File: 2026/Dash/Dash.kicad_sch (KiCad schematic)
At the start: 88 parts, among them IC1 ESP32-S3-WROOM-1-N8R8, IC2 CP2102N-A02-GQFN28, IC3 TLP175A_TPL,E, IC4 TPS2116DRLR, IC5 MIC37100-3.3WS, IC6 TLC5955RTQT, IC7 TLC5955RTQT, J2 USB_C_Receptacle_USB2.0_16P, J5 Conn_01x40_Pin, Q1 MMBT2222LT1G, Q2 MMBT2222LT1G, U1 USBLC6-2SC6, U2 SN65HVD230

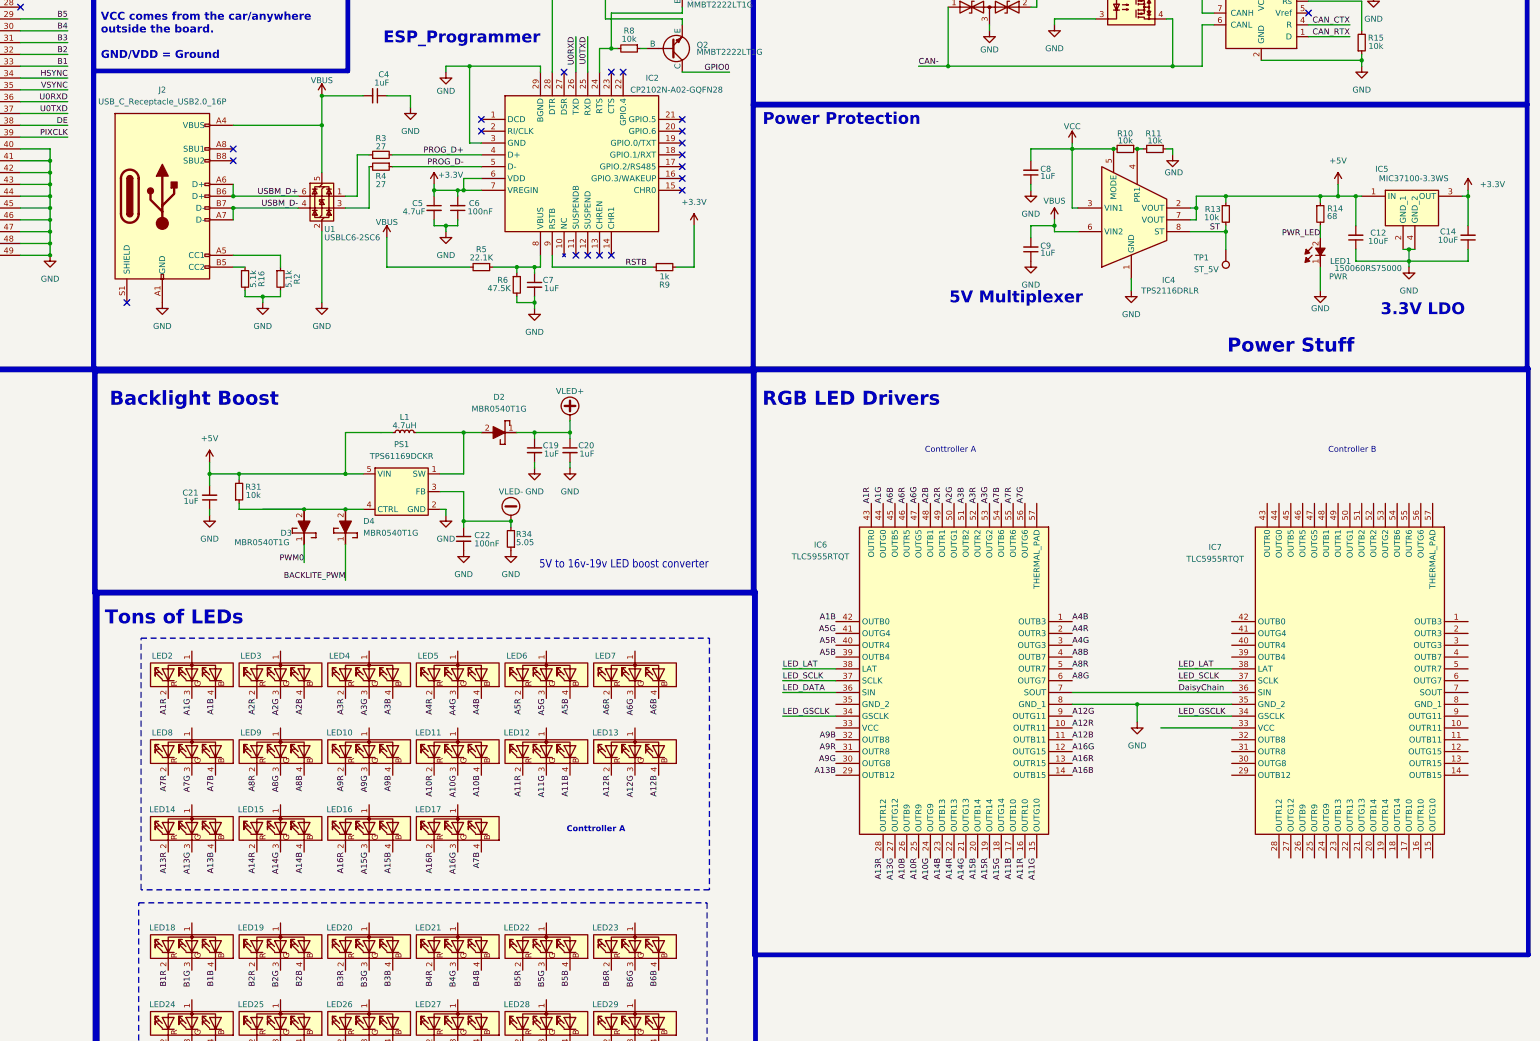
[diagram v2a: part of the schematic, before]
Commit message: Changed dash to IP67 USB C
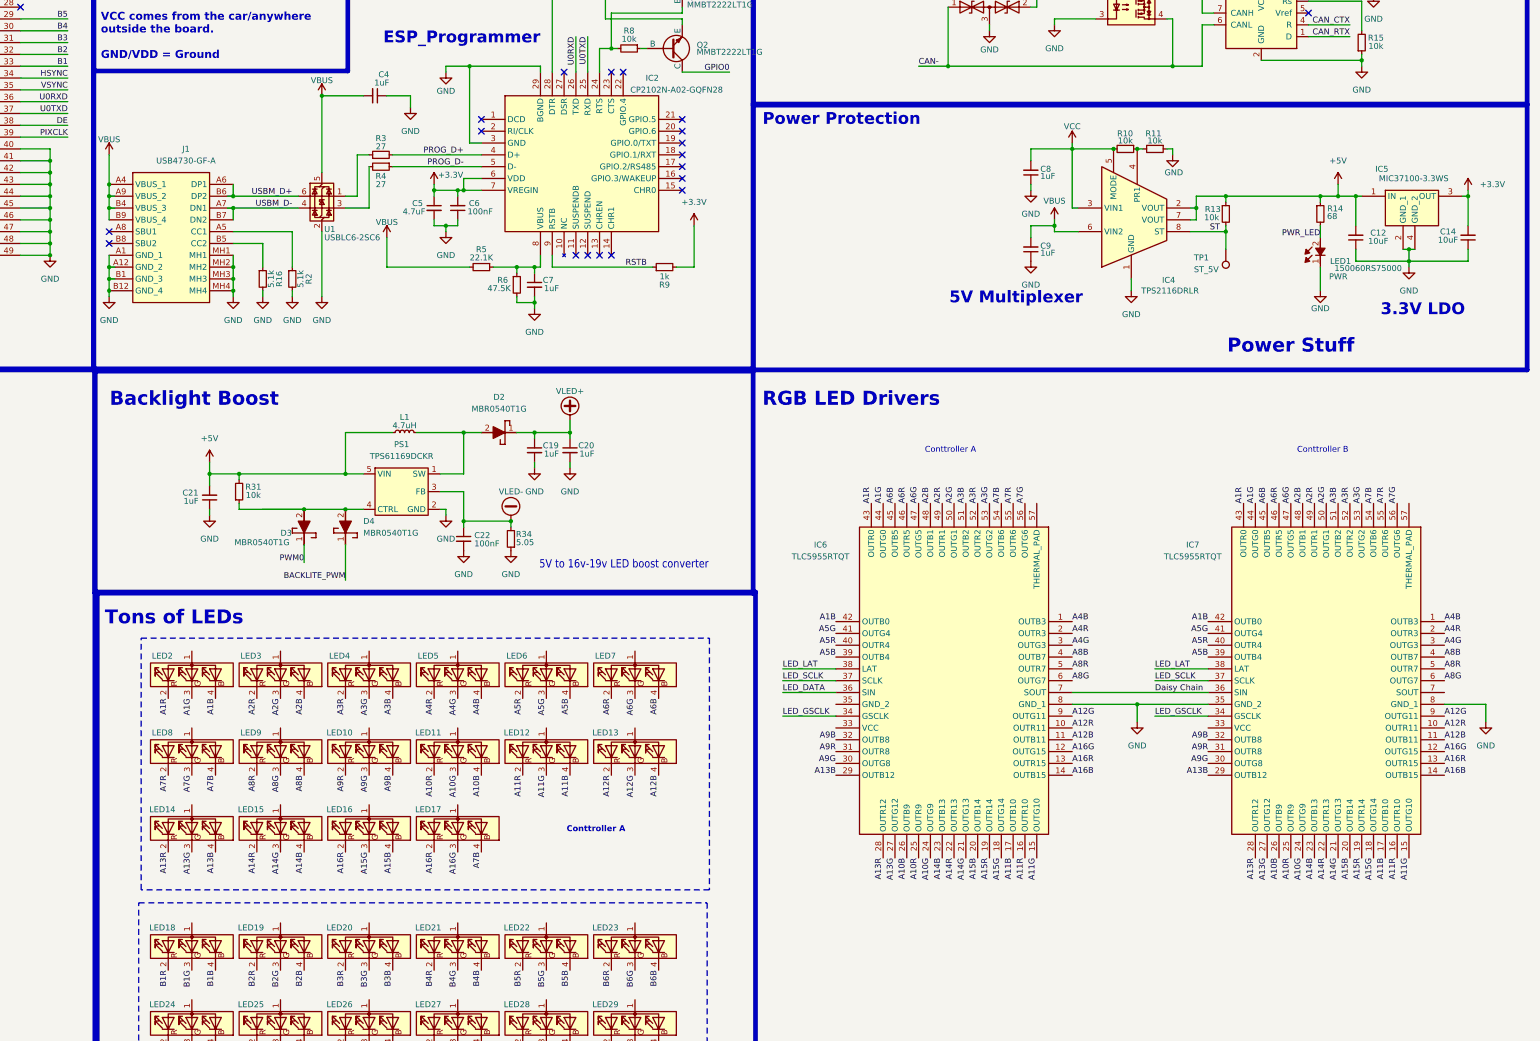
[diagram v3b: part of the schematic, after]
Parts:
- removed J2: USB_C_Receptacle_USB2.0_16P, SDM_MiscFootprint:USB_C_Receptacle_16P, symbol Connector:USB_C_Receptacle_USB2.0_16P
- added J1: USB4730-GF-A, USB4730GFA, symbol SDM_CONNECTOR:USB4730-GF-A
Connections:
- net A10B: now also IC7.26 (OUTB9)
- net A10G: now also IC7.24 (OUTG9)
- net A10R: now also IC7.25 (OUTR9)
- net A11B: now also IC7.17 (OUTB10)
- net A11G: now also IC7.15 (OUTG10)
- net A11R: now also IC7.16 (OUTR10)
- net A12B: now also IC7.11 (OUTB11)
- net A12G: now also IC7.9 (OUTG11)
- net A12R: now also IC7.10 (OUTR11)
- net A13B: now also IC7.29 (OUTB12)
- net A13G: now also IC7.27 (OUTG12)
- net A13R: now also IC7.28 (OUTR12)
- net A14B: now also IC7.23 (OUTB13)
- net A14G: now also IC7.21 (OUTG13)
- net A14R: now also IC7.22 (OUTR13)
- net A15B: now also IC7.20 (OUTB14)
- net A15G: now also IC7.18 (OUTG14)
- net A15R: now also IC7.19 (OUTR14)
- net A16B: now also IC7.14 (OUTB15)
- net A16G: now also IC7.12 (OUTG15)
- net A16R: now also IC7.13 (OUTR15)
- net A1B: now also IC7.42 (OUTB0)
- net A1G: now also IC7.44 (OUTG0)
- net A1R: now also IC7.43 (OUTR0)
- net A2B: now also IC7.48 (OUTB1)
- net A2G: now also IC7.50 (OUTG1)
- net A2R: now also IC7.49 (OUTR1)
- net A3B: now also IC7.51 (OUTB2)
- net A3G: now also IC7.53 (OUTG2)
- net A3R: now also IC7.52 (OUTR2)
- net A4B: now also IC7.1 (OUTB3)
- net A4G: now also IC7.3 (OUTG3)
- net A4R: now also IC7.2 (OUTR3)
- net A5B: now also IC7.39 (OUTB4)
- net A5G: now also IC7.41 (OUTG4)
- net A5R: now also IC7.40 (OUTR4)
- net A6B: now also IC7.45 (OUTB5)
- net A6G: now also IC7.47 (OUTG5)
- net A6R: now also IC7.46 (OUTR5)
- net A7B: now also IC7.54 (OUTB6)
- net A7G: now also IC7.56 (OUTG6)
- net A7R: now also IC7.55 (OUTR6)
- net A8B: now also IC7.4 (OUTB7)
- net A8G: now also IC7.6 (OUTG7)
- net A8R: now also IC7.5 (OUTR7)
- net A9B: now also IC7.32 (OUTB8)
- net A9G: now also IC7.30 (OUTG8)
- net A9R: now also IC7.31 (OUTR8)
- net GND: now also IC7.8 (GND_1), J1.A1 (GND_1), J1.A12 (GND_2), J1.B1 (GND_3), J1.B12 (GND_4), J1.MH1, J1.MH2, J1.MH3, J1.MH4
- net USBM_D+: now also J1.A6 (DP1), J1.B6 (DP2)
- net USBM_D-: now also J1.A7 (DN1), J1.B7 (DN2)
- net VBUS: now also J1.A4 (VBUS_1), J1.A9 (VBUS_2), J1.B4 (VBUS_3), J1.B9 (VBUS_4)
- net at R2.1: now also J1.A5 (CC1)
- net at R16.1: now also J1.B5 (CC2)
- net DaisyChain renamed Daisy Chain
- no-connect marks 24 -> 23
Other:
- note added: "Conttroller B"
- moved on the sheet: R2

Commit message: Dash progress
added to libs and swaped dash to BT818. Work in progress
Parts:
- removed J5: Conn_01x40_Pin, Connector_FFC-FPC:Omron_XF2M-4015-1A_1x40-1MP_P0.5mm_Horizontal, symbol Connector:Conn_01x40_Pin
- added C10: O.1uF, Capacitor_SMD:C_0603_1608Metric, symbol Device:C_Small
- added IC8: BT818Q-T, SDM_MiscFootprint:QFN50P900X900X90-65N-D, symbol SDM_CONNECTOR:BT818Q-T
- added IC9: S25FL256LAGNFB010, SDM_MiscFootprint:SON127P600X500X80-9N-D, symbol SDM_CONNECTOR:S25FL256LAGNFB010
- added J2: Conn_01x40_Pin, Connector_FFC-FPC:Omron_XF2M-4015-1A_1x40-1MP_P0.5mm_Horizontal, symbol Connector:Conn_01x40_Pin
- added J4: Molex_1040310811, Connector_Card:microSD_HC_Molex_104031-0811, symbol Connector:Micro_SD_Card_Det2
- added R17, R18, R19, R20, R21, R22, R23, R24, R25, R26, R27, R28, R29, R30, R32, R33, R35, R36, R37, R38, R39, R40, R41, R42, R43, R44, R45, R46, R47, R48, R49, R50, R52, R53: 33, Resistor_SMD:R_0603_1608Metric, symbol Device:R_Small
- added R51: 47K, Resistor_SMD:R_0603_1608Metric, symbol Device:R_Small
- added U10: EMIF06-MSD02N16, SDM_MiscFootprint:UQFN-17-3.5x1.2mm_copy, symbol lib:ST_EMIF06-MSD02N16
- J1: footprint USB4730GFA -> SDM_MiscFootprint:USB4730GFA
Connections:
- net SD_MISO is gone; now on net SD_CS: IC1.8 (IO15)
- net +3.3V: now also C10.2, IC8.17 (VCCIO3), IC9.8 (VCC), J2.4 (Pin_4), J4.4 (VDD), R51.2, U10.15 (VCC), U10.16 (RDATA_VCC)
- net B1: now also J2.22 (Pin_22), R20.2; no longer IC1.33 (IO40)
- net B2: now also J2.23 (Pin_23), R24.2; no longer IC1.32 (IO39)
- net B3: now also J2.24 (Pin_24), R25.2; no longer IC1.31 (IO38)
- net B4: now also J2.25 (Pin_25), R26.2; no longer IC1.30 (IO37)
- net B5: now also J2.26 (Pin_26), R27.2; no longer IC1.29 (IO36)
- net BACKLITE_PWM: now also IC8.34 (BACKLIGHT)
- net DE: now also IC8.35 (DE), J2.34 (Pin_34); no longer IC1.38 (IO2)
- net G0: now also J2.13 (Pin_13), R39.2; no longer IC1.25 (IO48)
- net G1: now also J2.14 (Pin_14), R38.2; no longer IC1.24 (IO47)
- net G2: now also J2.15 (Pin_15), R37.2; no longer IC1.23 (IO21)
- net G3: now also J2.16 (Pin_16), R36.2; no longer IC1.22 (IO14)
- net G4: now also J2.17 (Pin_17), R35.2; no longer IC1.21 (IO13)
- net G5: now also J2.18 (Pin_18), R33.2; no longer IC1.20 (IO12)
- net GND: now also C10.1, IC9.4 (VSS), IC9.9 (EP), J2.29 (Pin_29), J2.3 (Pin_3), J2.36 (Pin_36), J4.11 (SHIELD), J4.6 (VSS), J4.9 (DET_B), U10.17 (GND)
- net HSYNC: now also IC8.37 (HSYNC), J2.32 (Pin_32); no longer IC1.34 (IO41)
- net PIXCLK: now also IC8.39 (PCLK), J2.30 (Pin_30); no longer IC1.39 (IO1)
- net R1: now also J2.6 (Pin_6), R46.2; no longer IC1.19 (IO11)
- net R2: now also J2.7 (Pin_7), R45.2; no longer IC1.18 (IO10)
- net R3: now also J2.8 (Pin_8), R44.2; no longer IC1.17 (IO9)
- net R4: now also J2.9 (Pin_9), R43.2; no longer IC1.16 (IO46)
- net R5: now also J2.10 (Pin_10), R42.2; no longer IC1.15 (IO3)
- net SD_CS: no longer IC1.9 (IO16)
- net VLED+: now also J2.2 (Pin_2)
- net VLED-: now also J2.1 (Pin_1)
- net VSYNC: now also IC8.36 (VSYNC), J2.33 (Pin_33); no longer IC1.35 (IO42)
- net X+: now also IC8.29 (XP), J2.40 (Pin_40)
- net X-: now also IC8.31 (XM), J2.38 (Pin_38)
- net Y+: now also IC8.30 (YP), J2.37 (Pin_37)
- net Y-: now also IC8.32 (YM), J2.39 (Pin_39)
- net SD_MOSI: no longer names the net of IC1.7 (IO7)
- net SD_SCK: no longer names the net of IC1.6 (IO6)
- new net: IC9.3 (W_P#_/_IO_2), R22.1
- new net: IC8.19 (SPIM_IO2), R22.2
- new net: IC8.62 (R3), R44.1
- new net: IC8.63 (R2), R45.1
- new net: IC8.4 (MISO), R49.2
- new net: IC8.46 (B1), R20.1
- new net: IC8.55 (G1), R38.1
- new net: IC9.2 (SO/IO_1), R21.1
- new net: IC9.5 (SI_/_IO_0), R19.1
- new net: IC9.6 (SCK), R17.1
- new net: IC9.7 (IO_3_/_RESET#), R23.1
- new net: IC8.42 (B5), R27.1
- new net: IC8.44 (B3), R25.1
- new net: IC8.54 (G2), R37.1
- new net: IC8.59 (R6), R41.1
- new net: IC8.1 (R0), R47.1
- new net: IC8.61 (R4), R43.1
- new net: IC8.50 (G6), R32.1
- new net: IC8.41 (B6), R28.1
- new net: IC8.52 (G4), R35.1
- new net: IC8.40 (B7), R29.1
- new net: IC8.18 (SPIM_MISO), R21.2
- new net: IC8.45 (B2), R24.1
- new net: IC8.5 (MOSI), R50.2
- new net: IC8.16 (SPIM_MOSI), R19.2
- new net: IC8.20 (SPIM_IO3), R23.2
- new net: IC8.7 (GPIO0/IO2), R52.2
- new net: IC8.64 (R1), R46.1
- new net: IC8.14 (SPIM_SCLK), R17.2
- new net: IC8.49 (G7), R30.1
- new net: IC8.51 (G5), R33.1
- new net: IC8.58 (R7), R40.1
- new net: IC8.60 (R5), R42.1
- new net: IC8.43 (B4), R26.1
- new net: IC8.53 (G3), R36.1
- new net: IC8.56 (G0), R39.1
- new net: J4.7 (DAT0), U10.10 (DAT0_EX)
- new net: J4.5 (CLK), U10.11 (CLK_EX)
- new net: J4.3 (CMD), U10.12 (CMD_EX)
- new net: J4.2 (DAT3/CD), U10.13 (DAT3_EX)
- new net: J4.1 (DAT2), U10.14 (DAT2_EX)
- new net: J4.8 (DAT1), U10.9 (DAT1_EX)
- new net: IC8.3 (SCK), R48.2
- new net: IC8.47 (B0), R18.1
- new net: IC8.8 (GPIO1/IO3), R53.2
- new net B0: J2.21 (Pin_21), R18.2
- new net B6: J2.27 (Pin_27), R28.2
- new net B7: J2.28 (Pin_28), R29.2
- new net DISP: IC8.38 (DISP), J2.31 (Pin_31)
- new net DISP_CS: IC1.22 (IO14), IC8.6 (CS_N)
- new net G6: J2.19 (Pin_19), R32.2
- new net G7: J2.20 (Pin_20), R30.2
- new net NOR_CS: IC8.15 (SPIM_SS_N), IC9.1 (CS#), R51.1
- new net R0: J2.5 (Pin_5), R47.2
- new net R6: J2.11 (Pin_11), R41.2
- new net R7: J2.12 (Pin_12), R40.2
- new net SD_CD: IC1.23 (IO21), J4.10 (DET_A), U10.1 (WP/CD)
- new net SD_CMD: IC1.15 (IO3), U10.5 (CMD_IN)
- new net SPI_CLK: IC1.17 (IO9), R48.1, U10.6 (CLK_IN)
- new net SPI_DATA0: IC1.18 (IO10), R49.1, U10.7 (DAT0_IN)
- new net SPI_DATA1: IC1.19 (IO11), R50.1, U10.8 (DAT1_IN)
- new net SPI_DATA2: IC1.20 (IO12), R52.1, U10.3 (DAT2_IN)
- new net SPI_DATA3: IC1.21 (IO13), R53.1, U10.4 (DAT3_IN)
- no-connect marks 23 -> 39
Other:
- note added: "uSD Card"
- note removed: "Power Protection"
- moved on the sheet: C11, C12, C13, C14, C8, C9, D1, IC3, IC4, IC5, LED1, R10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
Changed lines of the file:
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@@
 	(generator "eeschema")
 	(generator_version "9.0")
-	(paper "A3")
+	(paper "A2")

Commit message: Dash Updates
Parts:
- removed D3: MBR0540T1G, SDM_MiscFootprint:SOD3716X135N, symbol SDM_DIODES:MBR0540T1G
- added BLACK_TP1: 5006, SDM_MiscFootprint:5006, symbol SDM_TESTPOINT:5006
- added C15, C16, C17, C18: 100nF, Capacitor_SMD:C_0603_1608Metric, symbol Device:C_Small
- added C23, C24, C26: 22uF, Capacitor_SMD:C_0603_1608Metric, symbol Device:C_Small
- added C25: 47uF, Capacitor_SMD:CP_Elec_6.3x5.9, symbol Device:C_Small
- added C27: 1uF, Capacitor_SMD:C_0603_1608Metric, symbol Device:C_Small
- added IC10: TPS563211DRLR, SDM_MiscFootprint:SOTFL50P160X60-8N, symbol SDM_VOLTAGE_REGULATORS:TPS563211DRLR
- added J3: 19428-0011, 194280011, symbol SDM_CONNECTOR:19428-0011
- added L2: 4.7uH, Inductor_SMD:L_Bourns_SRP7028A_7.3x6.6mm, symbol Device:L_Small
- added R54, R57, R58, R59, R60: 10k, Resistor_SMD:R_0603_1608Metric, symbol Device:R_Small
- added R55: 82k, Resistor_SMD:R_0603_1608Metric, symbol Device:R_Small
- added R56: 11k, Resistor_SMD:R_0603_1608Metric, symbol Device:R_Small
- added S1, S2, S3, S4: KSS321G_LFS, SDM_MiscFootprint:KSS321GLFS, symbol SDM_CONNECTOR:KSS321G_LFS
- added TP2: SMPS, TestPoint:TestPoint_Pad_1.5x1.5mm, symbol Connector:TestPoint
- C10: value O.1uF -> 100nF
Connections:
- net +3.3V: now also IC8.24 (VCC), IC8.27 (VCCA), IC8.28 (VCCIO2), IC8.9 (VCCIO1), C15.2, C16.2, C17.2, S1.1, S2.1, S3.1, S4.1
- net A13G: no longer IC7.27 (OUTG12)
- net A13R: no longer IC7.28 (OUTR12)
- net B13G: now also IC7.27 (OUTG12)
- net B13R: now also IC7.28 (OUTR12)
- net BACKLITE_PWM: now also IC8.10 (GPIO2); no longer D4.1 (K), IC8.34 (BACKLIGHT)
- net CAN+: now also J3.1
- net CAN-: now also J3.3
- net GND: now also IC8.23 (GND_1), IC8.33 (GND_2), IC8.48 (GND_3), IC8.65 (GND_4), BLACK_TP1.1, C15.1, C16.1, C17.1, C23.2, C24.2, C25.1, C26.1, C27.1, IC10.4 (GND), J3.4, R56.2, R57.2, R58.2, R59.2, R60.2
- net PWM0: now also D4.1 (K), IC8.34 (BACKLIGHT)
- net VCC: now also C23.1, C24.1, L2.1, R54.2, R55.1, TP2.1
- net BTN1: now reaches IC1.28 (IO35)
- net BTN1: now also R57.1, S1.2
- net BTN2: now reaches IC1.29 (IO36)
- net BTN2: now also R58.1, S2.2
- net BTN3: now reaches IC1.30 (IO37)
- net BTN3: now also R59.1, S3.2
- net BTN4: now reaches IC1.31 (IO38)
- net BTN4: now also R60.1, S4.2
- net INT_N: now reaches IC1.6 (IO6)
- net INT_N: now also IC8.11 (INT_N)
- net PD_N: now reaches IC1.7 (IO7)
- net PD_N: now also IC8.12 (PD_N)
- new net +BATT: C25.2, C26.2, C27.2, IC10.2 (VIN), J3.2
- new net BTSB: C18.1, IC10.5 (BOOT)
- new net PG: IC10.1 (PG/SS), R54.1
- new net SMPS_FB: IC10.8 (FB), R55.2, R56.1
- new net SMPS_SW: C18.2, IC10.3 (SW), L2.2
- no-connect marks 39 -> 40
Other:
- note added: "40p Display Connector"
- note added: "4PIN, CAN+ CAN- 12V GND"
- note added: "5V Switching Regulator"
- note added: "Buttons"
- note added: "Display Driver"
- note added: "SDM26 Custome Digital Dash"
- moved on the sheet: C11, C12, C13, C14, C19, C20, C21, C22, C8, C9, D1, D2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
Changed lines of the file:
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@@
 	(generator "eeschema")
 	(generator_version "9.0")
-	(paper "A2")
+	(paper "User" 390 450)

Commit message: Dash PCB work
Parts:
- J3: footprint 194280011 -> SDM_MiscFootprint:194280011
- U10: footprint SDM_MiscFootprint:UQFN-17-3.5x1.2mm_copy -> SDM_MiscFootprint:UQFN-17-3.5x1.2mm

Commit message: dash
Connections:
- net A15R: now also LED16.2 (R)
- net A16B: now also LED17.4 (B)
- net A16R: no longer LED16.2 (R)
- net A7B: no longer LED17.4 (B)
